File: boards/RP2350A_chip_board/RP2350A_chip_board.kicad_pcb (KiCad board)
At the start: 2 copper layers, 20 x 40 mm, 40 parts, among them J1 Conn_01x02, J2 Conn_01x03, J3 Conn_01x16, J4 Conn_01x03, J5 Conn_01x01, J6 Conn_01x01, U1 W25Q128JVS, U2 RP2350_60QFN, Y1 ABM8-272-T3

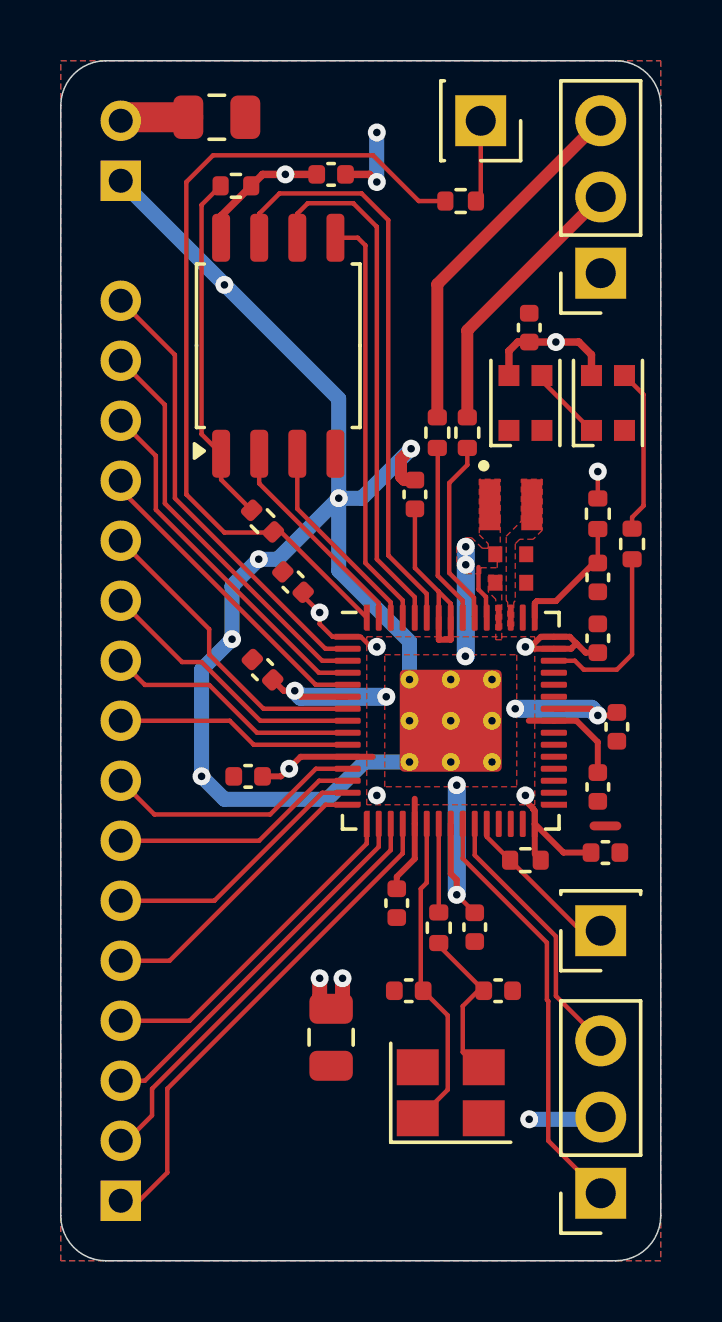
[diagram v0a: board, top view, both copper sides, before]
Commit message: Add Broker board
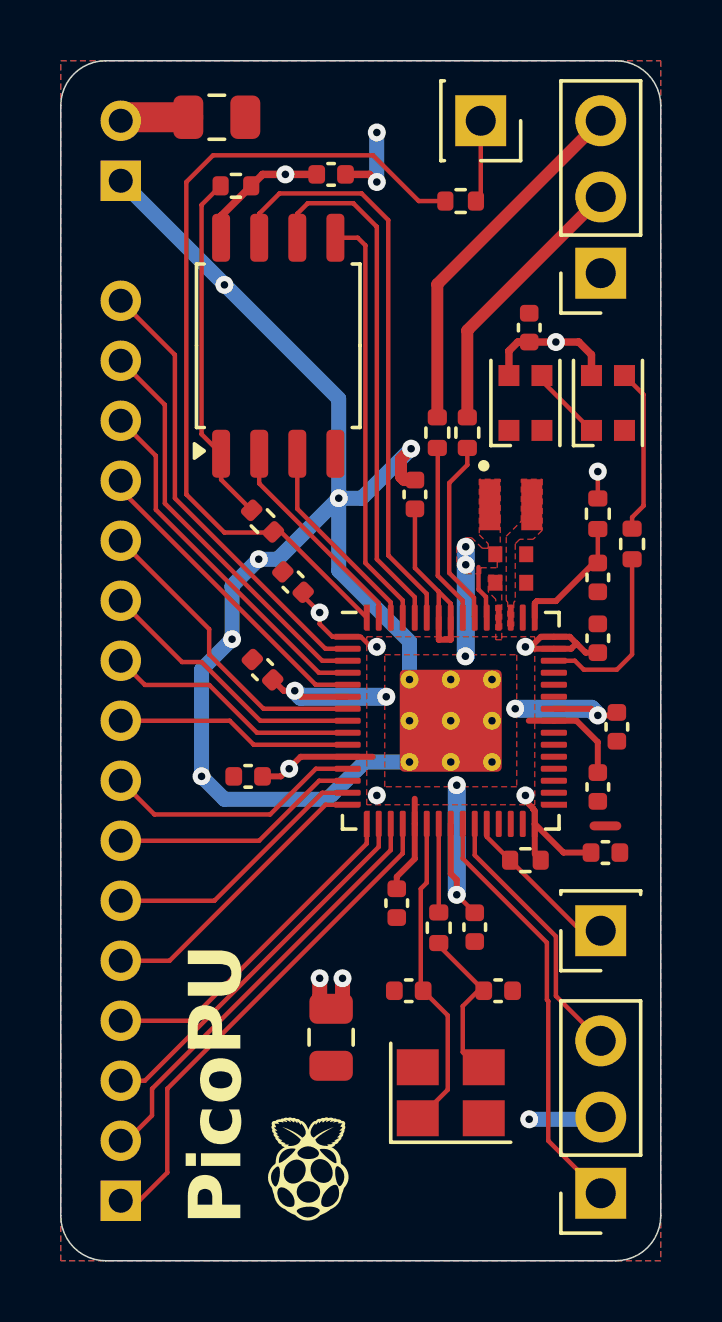
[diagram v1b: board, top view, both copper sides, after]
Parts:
- C12, C13: footprint RP2350_60QFN_minimal:C_0402_1005Metric_small_pads -> RP2350A_chip_board:C_0402_1005Metric_small_pads
- L1: footprint RP2350_60QFN_minimal:L_pol_2016 -> RP2350A_chip_board:L_pol_2016
- U2: footprint RP2350_60QFN_minimal:RP2350-QFN-60-1EP_7x7_P0.4mm_EP3.4x3.4mm_ThermalVias -> RP2350A_chip_board:RP2350-QFN-60-1EP_7x7_P0.4mm_EP3.4x3.4mm_ThermalVias
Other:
- board text added: "PicoPU"
